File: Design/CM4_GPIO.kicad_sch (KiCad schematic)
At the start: 28 parts, among them J1 Conn_01x03, J2 Conn_02x07_Odd_Even, J3 Conn_01x03, J7 Micro_SD_Card_Det, J8 THD-20-R, J9 THD-02-R, U1 TPD4EUSB30, U18 RT9742GGJ5, U2 TPD4EUSB30, U3 MagJack-A70-112-331N126, U5 74LVC1G07SE-7, U9 74LVC1G07SE-7

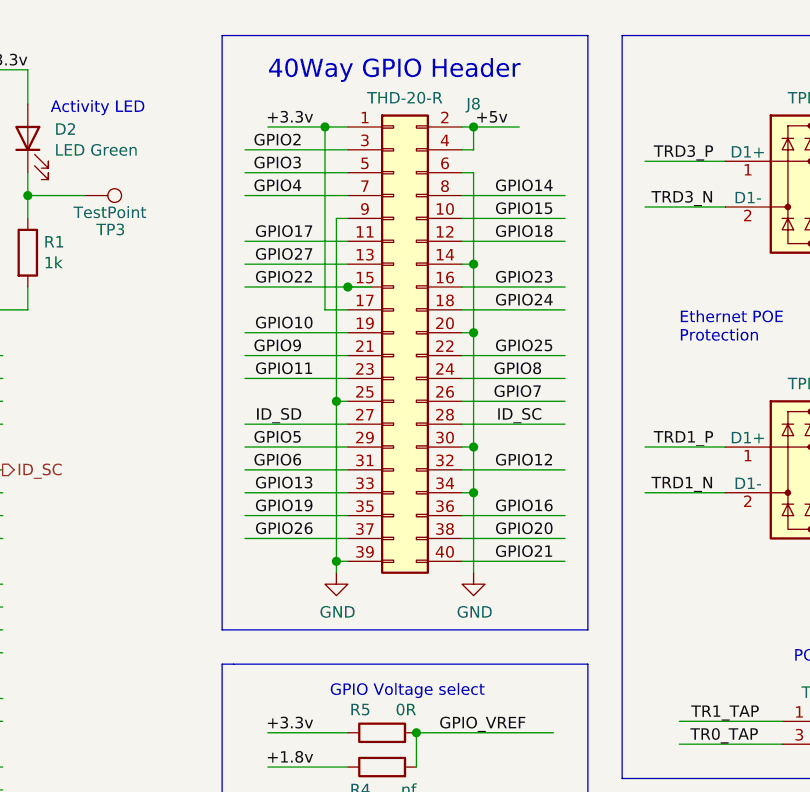
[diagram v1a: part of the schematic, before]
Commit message: 40-way header removed
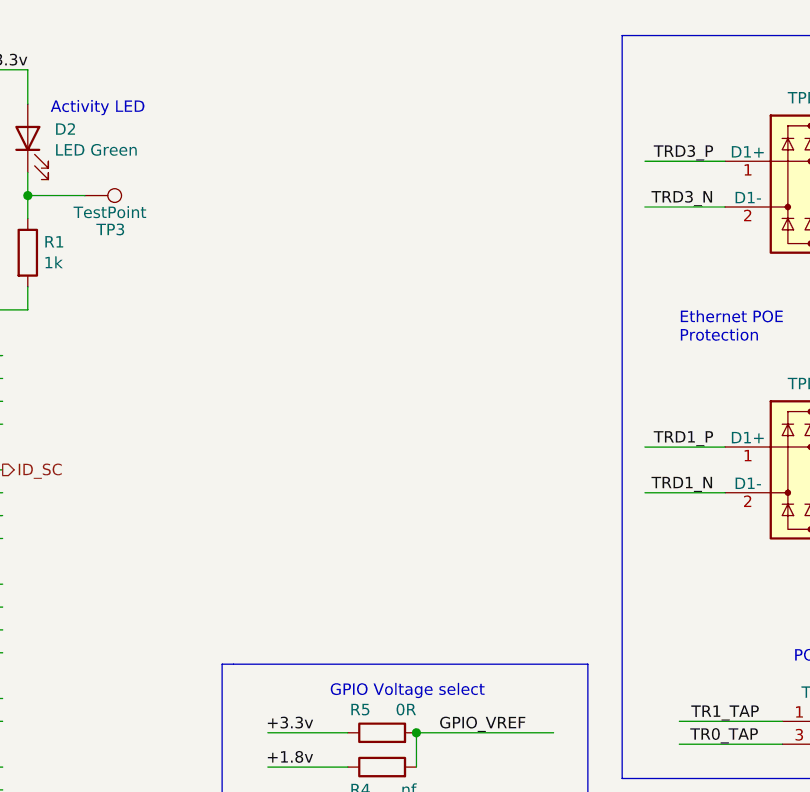
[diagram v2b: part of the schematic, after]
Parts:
- removed J8: THD-20-R, Connector_PinHeader_2.54mm:PinHeader_2x20_P2.54mm_Vertical, symbol Connector_Generic:Conn_02x20_Odd_Even
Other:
- note removed: "40Way GPIO Header"

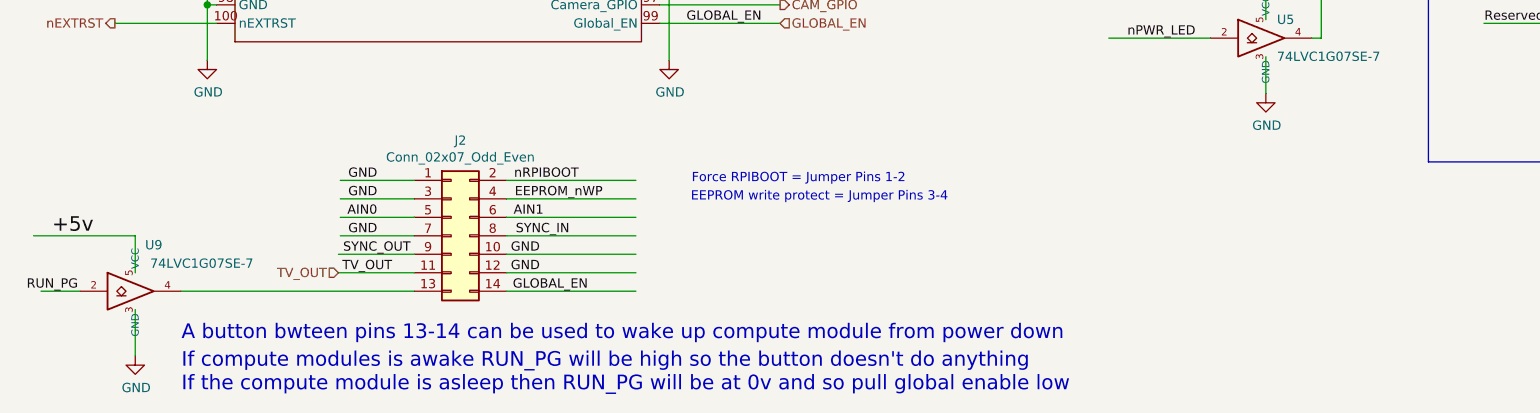
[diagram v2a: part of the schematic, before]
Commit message: J2 header removed from schematics
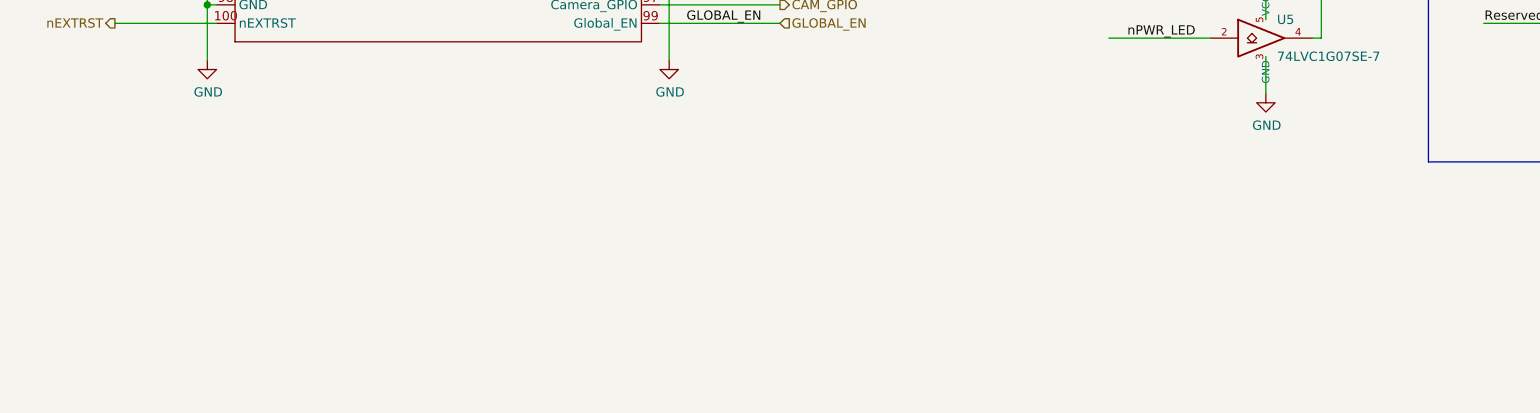
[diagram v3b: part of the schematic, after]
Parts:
- removed J2: Conn_02x07_Odd_Even, Connector_PinHeader_2.54mm:PinHeader_2x07_P2.54mm_Vertical, symbol Connector_Generic:Conn_02x07_Odd_Even
- removed U9: 74LVC1G07SE-7, Package_TO_SOT_SMD:SOT-353_SC-70-5, symbol CM4IO:74LVC1G07_copy
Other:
- note removed: "A button bwteen pins 13-14 can be used to wake up compute module from power down"
- note removed: "EEPROM write protect = Jumper Pins 3-4"
- note removed: "Force RPIBOOT = Jumper Pins 1-2"
- note removed: "If compute modules is awake RUN_PG will be high so the button doesn't do anything If the compute module is asleep then RUN_PG will be at 0v and so pull global enable low"
